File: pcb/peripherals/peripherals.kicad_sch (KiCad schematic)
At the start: 14 parts, among them J1 JST XH, J10 Conn_01x04, J2 JST XH, J3 JST XH, J4 Conn_01x08, J9 Conn_01x08, U1 Arduino_Nano_v3.x

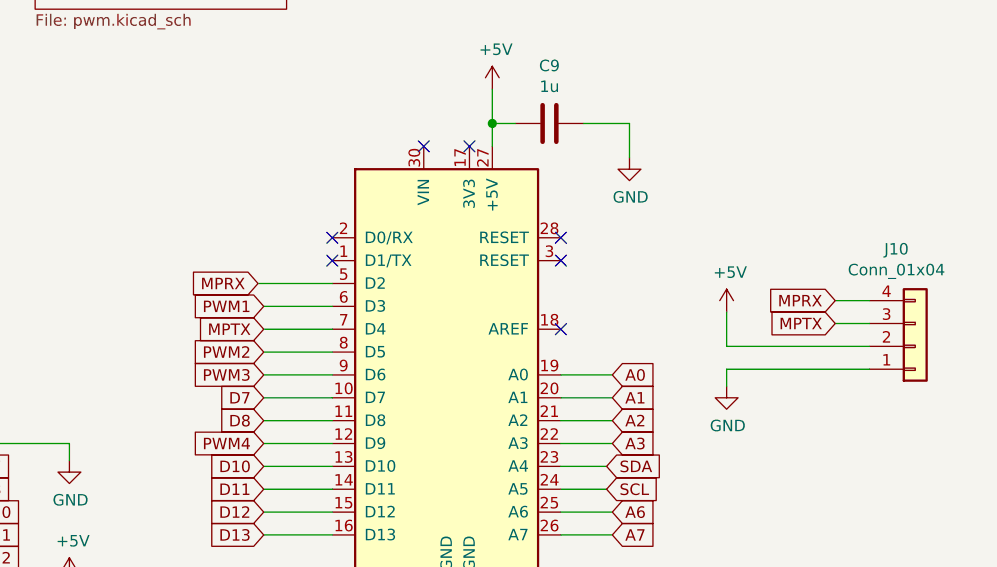
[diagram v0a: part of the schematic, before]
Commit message: Route UART to J10.
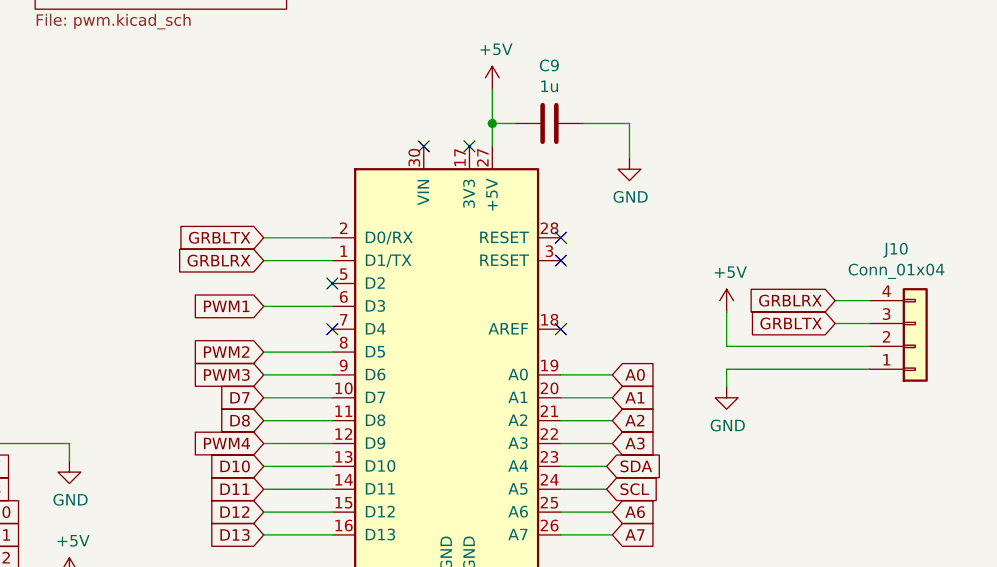
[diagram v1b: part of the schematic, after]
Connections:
- net GRBLRX: now reaches U1.1 (D1/TX)
- net GRBLRX: now also J10.4 (Pin_4)
- net GRBLTX: now reaches U1.2 (D0/RX)
- net GRBLTX: now also J10.3 (Pin_3)
- net MPRX: no longer names the net of U1.5 (D2)
- net MPRX: no longer J10.4 (Pin_4)
- net MPTX: no longer names the net of U1.7 (D4)
- net MPTX: no longer J10.3 (Pin_3)
